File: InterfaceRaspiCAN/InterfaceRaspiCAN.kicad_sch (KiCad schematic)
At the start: 31 parts, among them J1 Raspberry_Pi_2_3, J10 Conn_02x01, J11 Conn_02x01, J12 Conn_02x01, J13 Conn_01x02, J14 Conn_01x02, J15 Conn_01x02, J16 Conn_01x02, J2 CAN1, J3 CAN2, J4 I2C1_5, J5 I2C2_5, U1 MCP2517FD-xSL, U2 MCP2558FD-xSN, U3 PCF8574A, U4 PESD1CAN, Y2 40MHz

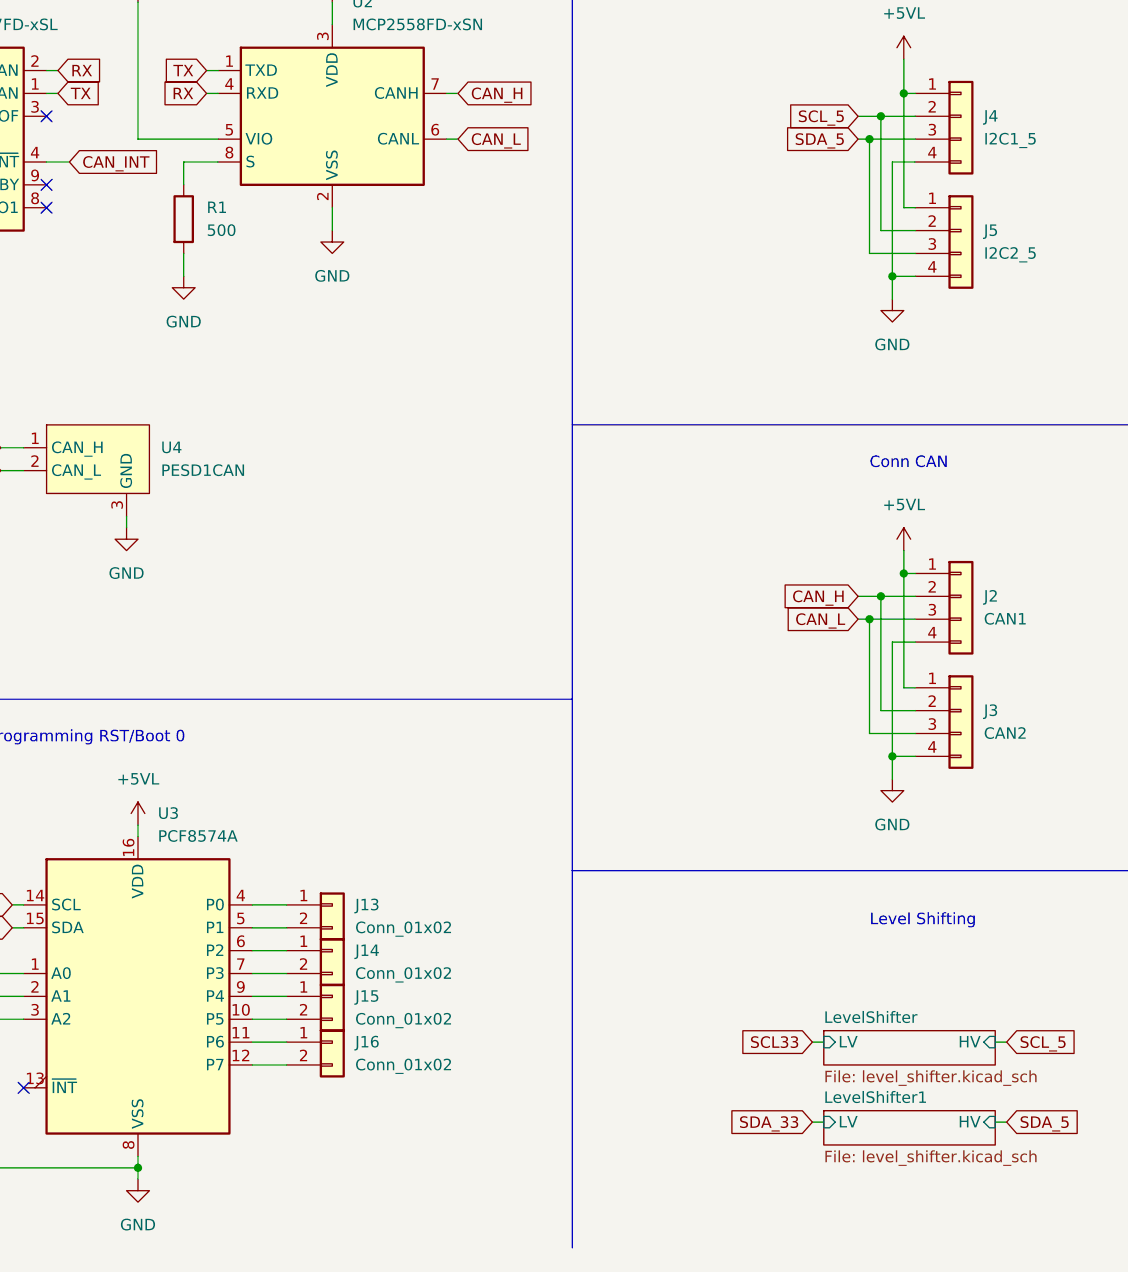
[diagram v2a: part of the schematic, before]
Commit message: Modification for InterfaceRaspiCAN
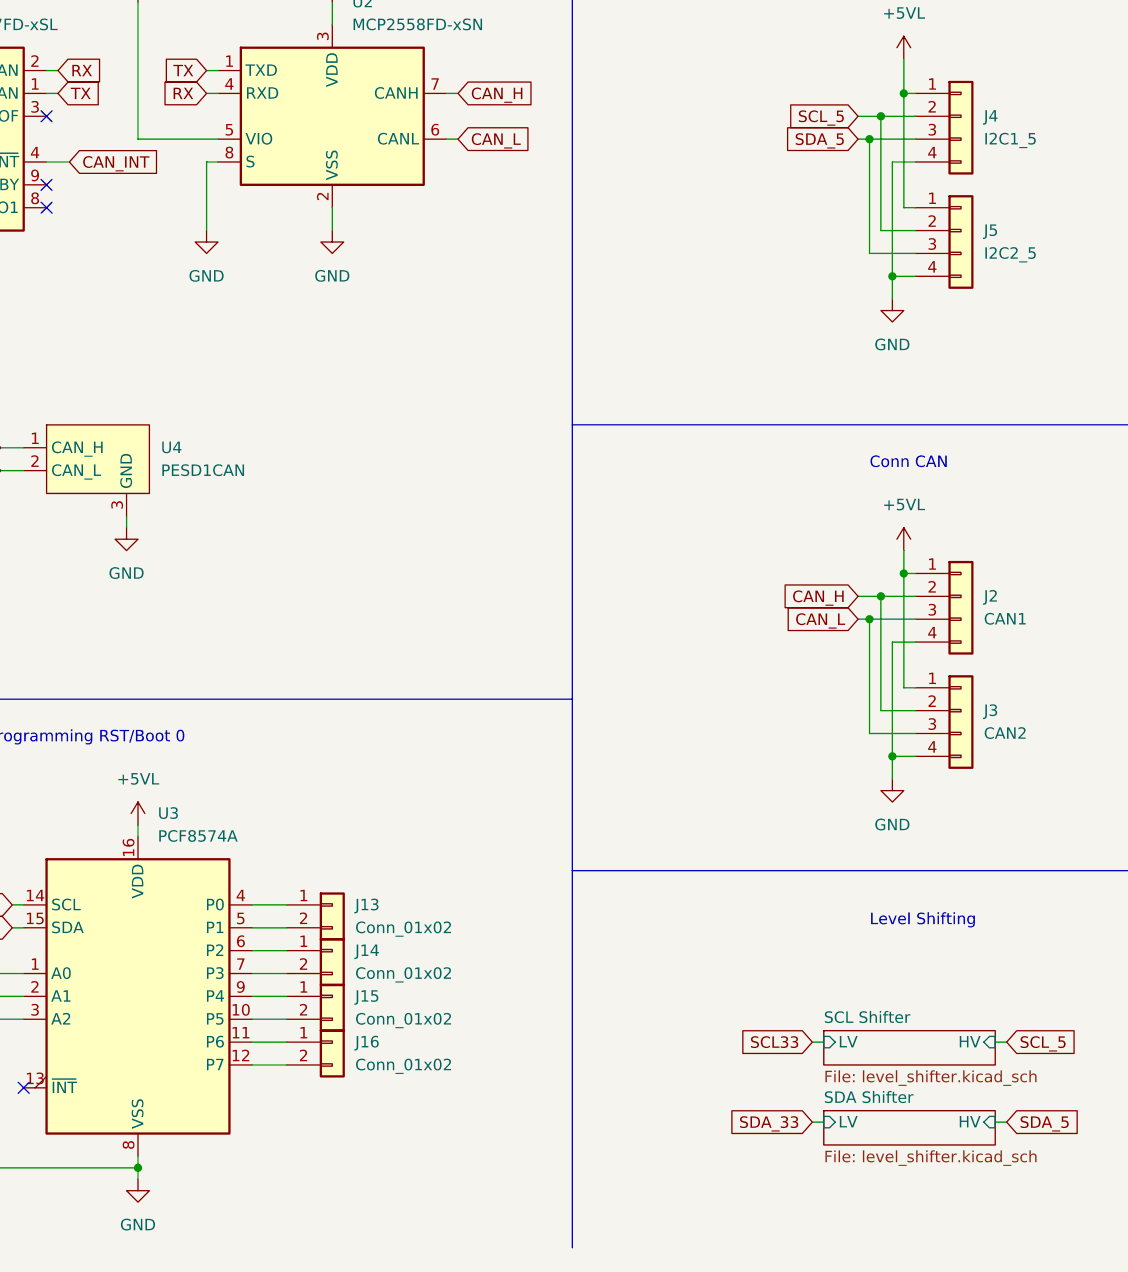
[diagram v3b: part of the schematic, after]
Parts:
- removed R1: 500, Resistor_SMD:R_0805_2012Metric_Pad1.20x1.40mm_HandSolder, symbol Device:R
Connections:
- net GND: now also U2.8 (S)
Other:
- sheet LevelShifter renamed SCL Shifter
- sheet LevelShifter1 renamed SDA Shifter
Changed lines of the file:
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@@
-    (stroke (width 0) (type default))
-  )
-  (wire (pts (xy 176.53 44.45) (xy 172.72 44.45))
     (stroke (width 0) (type default))
   )
@@
     (stroke (width 0) (type default))
   )
+  (wire (pts (xy 175.26 44.45) (xy 175.26 52.07))
+    (stroke (width 0) (type default))
+  )
   (wire (pts (xy 57.15 140.97) (xy 54.61 140.97))
     (stroke (width 0) (type default))
@@
     (stroke (width 0) (type default))
   )
-  (wire (pts (xy 172.72 44.45) (xy 172.72 46.99))
+  (wire (pts (xy 176.53 44.45) (xy 175.26 44.45))
     (stroke (width 0) (type default))
   )
@@
   )
   (wire (pts (xy 124.46 36.83) (xy 127 36.83))
-    (stroke (width 0) (type default))
-  )
-  (wire (pts (xy 172.72 54.61) (xy 172.72 57.15))
     (stroke (width 0) (type default))
   )
@@
     )
   )
+  (symbol (lib_id "power:GND") (at 175.26 52.07 0) (unit 1)
+    (in_bom yes) (on_board yes) (dnp no) (fields_autoplaced)
+    (property "Reference" "#PWR018" (at 175.26 58.42 0)
+      (effects (font (size 1.27 1.27)) hide)
+    )
+    (property "Value" "GND" (at 175.26 57.15 0)
+      (effects (font (size 1.27 1.27)))
+    )
+    (property "Footprint" "" (at 175.26 52.07 0)
+      (effects (font (size 1.27 1.27)) hide)
+    )
+    (property "Datasheet" "" (at 175.26 52.07 0)
+      (effects (font (size 1.27 1.27)) hide)
+    )
+    (pin "1")
+    (instances
+      (project "InterfaceRaspiCAN"
+        (path "/466ed181-1b10-43ca-b8d2-18d3e4c6e8d6"
+          (reference "#PWR018") (unit 1)
+        )
+      )
+    )
+  )
   (symbol (lib_id "power:+5VL") (at 91.44 25.4 0) (unit 1)
     (in_bom yes) (on_board yes) (dnp no) (fields_autoplaced)
@@
     )
   )
-  (symbol (lib_id "power:GND") (at 172.72 57.15 0) (unit 1)
-    (in_bom yes) (on_board yes) (dnp no) (fields_autoplaced)
-    (property "Reference" "#PWR018" (at 172.72 63.5 0)
-      (effects (font (size 1.27 1.27)) hide)
-    )
-    (property "Value" "GND" (at 172.72 62.23 0)
-      (effects (font (size 1.27 1.27)))
-    )
-    (property "Footprint" "" (at 172.72 57.15 0)
-      (effects (font (size 1.27 1.27)) hide)
-    )
-    (property "Datasheet" "" (at 172.72 57.15 0)
-      (effects (font (size 1.27 1.27)) hide)
-    )
-    (pin "1")
-    (instances
-      (project "InterfaceRaspiCAN"
-        (path "/466ed181-1b10-43ca-b8d2-18d3e4c6e8d6"
-          (reference "#PWR018") (unit 1)
-        )
-      )
-    )
-  )
   (symbol (lib_id "Connector_Generic:Conn_01x02") (at 189.23 127 0) (unit 1)
     (in_bom yes) (on_board yes) (dnp no) (fields_autoplaced)
@@
         (path "/466ed181-1b10-43ca-b8d2-18d3e4c6e8d6"
           (reference "J2") (unit 1)
-        )
-      )
-    )
-  )
-  (symbol (lib_id "Device:R") (at 172.72 50.8 0) (unit 1)
-    (in_bom yes) (on_board yes) (dnp no) (fields_autoplaced)
-    (property "Reference" "R1" (at 175.26 49.53 0)
-      (effects (font (size 1.27 1.27)) (justify left))
-    )
-    (property "Value" "500" (at 175.26 52.07 0)
-      (effects (font (size 1.27 1.27)) (justify left))
-    )
-    (property "Footprint" "Resistor_SMD:R_0805_2012Metric_Pad1.20x1.40mm_HandSolder" (at 170.942 50.8 90)
-      (effects (font (size 1.27 1.27)) hide)
-    )
-    (property "Datasheet" "~" (at 172.72 50.8 0)
-      (effects (font (size 1.27 1.27)) hide)
-    )
-    (pin "1")
-    (pin "2")
-    (instances
-      (project "InterfaceRaspiCAN"
-        (path "/466ed181-1b10-43ca-b8d2-18d3e4c6e8d6"
-          (reference "R1") (unit 1)
         )
       )
@@
     (stroke (width 0.1524) (type solid))
     (fill (color 0 0 0 0.0000))
-    (property "Sheetname" "LevelShifter1" (at 243.84 149.1484 0)
+    (property "Sheetname" "SDA Shifter" (at 243.84 149.1484 0)
       (effects (font (size 1.27 1.27)) (justify left bottom))
     )
@@
     (stroke (width 0.1524) (type solid))
     (fill (color 0 0 0 0.0000))
-    (property "Sheetname" "LevelShifter" (at 243.84 140.2584 0)
+    (property "Sheetname" "SCL Shifter" (at 243.84 140.2584 0)
       (effects (font (size 1.27 1.27)) (justify left bottom))
     )

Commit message: Change inApp prog, CAN & I2C connectors
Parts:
- J13, J14: footprint Connector_JST:JST_EH_B2B-EH-A_1x02_P2.50mm_Vertical -> Connector_JST:JST_PH_S2B-PH-K_1x02_P2.00mm_Horizontal
- J15, J16: footprint Connector_JST:JST_EH_S2B-EH_1x02_P2.50mm_Horizontal -> Connector_JST:JST_PH_S2B-PH-K_1x02_P2.00mm_Horizontal
- J2, J4: footprint Connector_JST:JST_EH_B4B-EH-A_1x04_P2.50mm_Vertical -> Connector_JST:JST_PH_S4B-PH-K_1x04_P2.00mm_Horizontal
- J3, J5: footprint Connector_JST:JST_EH_S4B-EH_1x04_P2.50mm_Horizontal -> Connector_JST:JST_PH_S4B-PH-K_1x04_P2.00mm_Horizontal
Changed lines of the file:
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@@
       (effects (font (size 1.27 1.27)) (justify left))
     )
-    (property "Footprint" "Connector_JST:JST_EH_S4B-EH_1x04_P2.50mm_Horizontal" (at 259.08 52.07 0)
+    (property "Footprint" "Connector_JST:JST_PH_S4B-PH-K_1x04_P2.00mm_Horizontal" (at 259.08 52.07 0)
       (effects (font (size 1.27 1.27)) hide)
     )
@@
       (effects (font (size 1.27 1.27)) (justify left))
     )
-    (property "Footprint" "Connector_JST:JST_EH_B2B-EH-A_1x02_P2.50mm_Vertical" (at 189.23 127 0)
+    (property "Footprint" "Connector_JST:JST_PH_S2B-PH-K_1x02_P2.00mm_Horizontal" (at 189.23 127 0)
       (effects (font (size 1.27 1.27)) hide)
     )
@@
       (effects (font (size 1.27 1.27)) (justify left))
     )
-    (property "Footprint" "Connector_JST:JST_EH_B4B-EH-A_1x04_P2.50mm_Vertical" (at 259.08 92.71 0)
+    (property "Footprint" "Connector_JST:JST_PH_S4B-PH-K_1x04_P2.00mm_Horizontal" (at 259.08 92.71 0)
       (effects (font (size 1.27 1.27)) hide)
     )
@@
       (effects (font (size 1.27 1.27)) (justify left))
     )
-    (property "Footprint" "Connector_JST:JST_EH_B4B-EH-A_1x04_P2.50mm_Vertical" (at 259.08 39.37 0)
+    (property "Footprint" "Connector_JST:JST_PH_S4B-PH-K_1x04_P2.00mm_Horizontal" (at 259.08 39.37 0)
       (effects (font (size 1.27 1.27)) hide)
     )
@@
       (effects (font (size 1.27 1.27)) (justify left))
     )
-    (property "Footprint" "Connector_JST:JST_EH_S2B-EH_1x02_P2.50mm_Horizontal" (at 189.23 142.24 0)
+    (property "Footprint" "Connector_JST:JST_PH_S2B-PH-K_1x02_P2.00mm_Horizontal" (at 189.23 142.24 0)
       (effects (font (size 1.27 1.27)) hide)
     )
@@
       (effects (font (size 1.27 1.27)) (justify left))
     )
-    (property "Footprint" "Connector_JST:JST_EH_S4B-EH_1x04_P2.50mm_Horizontal" (at 259.08 105.41 0)
+    (property "Footprint" "Connector_JST:JST_PH_S4B-PH-K_1x04_P2.00mm_Horizontal" (at 259.08 105.41 0)
       (effects (font (size 1.27 1.27)) hide)
     )
@@
       (effects (font (size 1.27 1.27)) (justify left))
     )
-    (property "Footprint" "Connector_JST:JST_EH_B2B-EH-A_1x02_P2.50mm_Vertical" (at 189.23 132.08 0)
+    (property "Footprint" "Connector_JST:JST_PH_S2B-PH-K_1x02_P2.00mm_Horizontal" (at 189.23 132.08 0)
       (effects (font (size 1.27 1.27)) hide)
     )
@@
       (effects (font (size 1.27 1.27)) (justify left))
     )
-    (property "Footprint" "Connector_JST:JST_EH_S2B-EH_1x02_P2.50mm_Horizontal" (at 189.23 137.16 0)
-      (effects (font (size 1.27 1.27)) hide)
-    )
+    (property "Footprint" "Connector_JST:JST_PH_S2B-PH-K_1x02_P2.00mm_Horizontal" (at 189.23 137.16 0)
+      (effects (font (size 1.27 1.27)) hide)
+    )
